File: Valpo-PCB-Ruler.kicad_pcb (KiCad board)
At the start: 2 copper layers, 203.2 x 38.1 mm, 6 parts

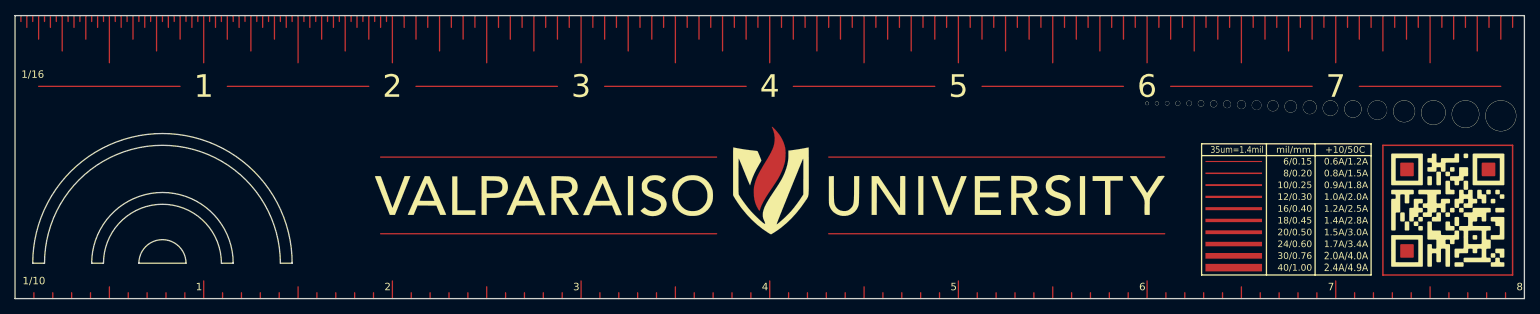
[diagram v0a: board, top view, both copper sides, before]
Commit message: Added Resistor Code + Transistors
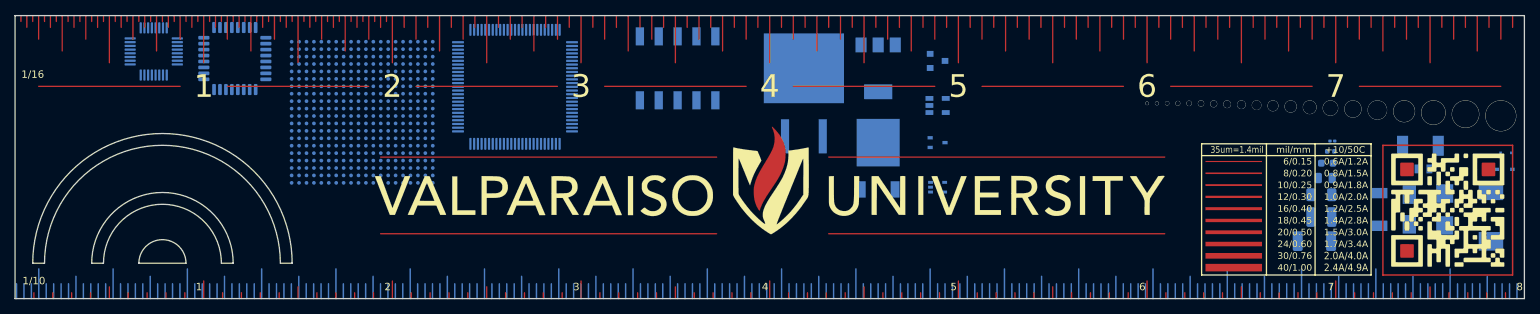
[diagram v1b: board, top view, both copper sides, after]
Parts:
- added 0603: R_0201_0603Metric, Resistor_SMD:R_0201_0603Metric, B.Cu at (228.1, 80.4)
- added 1005: R_0402_1005Metric, Resistor_SMD:R_0402_1005Metric, B.Cu at (227.9, 81.8)
- added 1608: R_0603_1608Metric, Resistor_SMD:R_0603_1608Metric, B.Cu at (227.4, 83.4)
- added 2012: R_0805_2012Metric, Resistor_SMD:R_0805_2012Metric, B.Cu at (227.2, 85.4)
- added 3216: R_1206_3216Metric, Resistor_SMD:R_1206_3216Metric, B.Cu at (226.7, 87.6)
- added 3225: R_1210_3225Metric, Resistor_SMD:R_1210_3225Metric, B.Cu at (226.7, 90.6)
- added 5025: R_2010_5025Metric, Resistor_SMD:R_2010_5025Metric, B.Cu at (225.7, 93.9)
- added BGA 20x20 1.0mm Pitch: BGA-400_21.0x21.0mm_Layout20x20_P1.0mm, Package_BGA:BGA-400_21.0x21.0mm_Layout20x20_P1.0mm, B.Cu at (97.5, 76.5)
- added MELF: D_MELF, Diode_SMD:D_MELF, B.Cu at (240.0, 81.0)
- added MicroMELF: D_MicroMELF, Diode_SMD:D_MicroMELF, B.Cu at (240.4, 84.1)
- added QFP32: LQFP-32_5x5mm_P0.5mm, Package_QFP:LQFP-32_5x5mm_P0.5mm, B.Cu at (69.5, 68.3)
- added QFP32: LQFP-32_7x7mm_P0.8mm, Package_QFP:LQFP-32_7x7mm_P0.8mm, B.Cu at (80.4, 69.3)
- added QPF100: LQFP-100_14x14mm_P0.5mm, Package_QFP:LQFP-100_14x14mm_P0.5mm, B.Cu at (118.1, 73.1)
- added SC80: D_SC-80, Diode_SMD:D_SC-80, B.Cu at (251.5, 82.0)
- added SMA: D_SMA, Diode_SMD:D_SMA, B.Cu at (238.5, 89.6)
- added SMB: D_SMB, Diode_SMD:D_SMB, B.Cu at (243.3, 89.6)
- added SMC: D_SMC, Diode_SMD:D_SMC, B.Cu at (249.5, 90.5)
- added SOD 128: D_SOD-128, Diode_SMD:D_SOD-128, B.Cu at (234.5, 89.6)
- added SOD 323: D_SOD-323, Diode_SMD:D_SOD-323, B.Cu at (251.3, 84.2)
- added SOT223: SOT-223, Package_TO_SOT_SMD:SOT-223, B.Cu at (167.0, 70.6)
- added SOT23: SOT-23, Package_TO_SOT_SMD:SOT-23, B.Cu at (175.0, 69.6)
- added SOT23-5: SOT-23-5, Package_TO_SOT_SMD:SOT-23-5, B.Cu at (175.0, 75.6)
- added SOT323: SOT-353_SC-70-5, Package_TO_SOT_SMD:SOT-353_SC-70-5, B.Cu at (175.0, 86.6)
- added SOT323: SOT-323_SC-70, Package_TO_SOT_SMD:SOT-323_SC-70, B.Cu at (175.0, 80.6)
- added SW_DIP_SPSTx05: SW_DIP_SPSTx05_Slide_9.78x14.88mm_W8.61mm_P2.54mm, Button_Switch_SMD:SW_DIP_SPSTx05_Slide_9.78x14.88mm_W8.61mm_P2.54mm, B.Cu at (140.0, 70.6)
- added TO252: TO-252-2, Package_TO_SOT_SMD:TO-252-2, B.Cu at (167.0, 82.7)
- added TO263: TO-263-2, Package_TO_SOT_SMD:TO-263-2, B.Cu at (157.0, 74.0)
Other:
- board text added: "0"
- board text added: "0.01Ω"
- board text added: "0.05%"
- board text added: "0.10%"
- board text added: "0.1Ω"
- board text added: "0.25%"
- board text added: "0.50%"
- board text added: "0.5mm Pitch"
- board text added: "0.8mm Pitch"
- board text added: "1%"
- board text added: "10%"
- board text added: "100KΩ"
- board text added: "100MΩ"
- board text added: "100Ω"
- board text added: "10KΩ"
- board text added: "10MΩ"
- board text added: "10Ω"
- board text added: "1GΩ"
- board text added: "1KΩ"
- board text added: "1MΩ"
- board text added: "1Ω"
- board text added: "2%"
- board text added: "5%"
- board text added: "Black"
- board text added: "Blue"
- board text added: "Brown"
- board text added: "D2PAK"
- board text added: "DPAK"
- board text added: "Diodes"
- board text added: "Gold"
- board text added: "Green"
- board text added: "Grey"
- board text added: "Orange"
- board text added: "RLC-Metric"
- board text added: "Red"
- board text added: "Resistor Color Code"
- board text added: "SC70"
- board text added: "SC73"
- board text added: "Silver"
- board text added: "Transistors"
- board text added: "Violet"
- board text added: "White"
- board text added: "Yellow"

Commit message: Added Protractor Markings
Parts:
- added G*** (x2): LOGO, Valpo-PCB-Ruler-FP:10_Deg_FP, F.Cu at (73.8, 96.1)
- added G***: LOGO, Valpo-PCB-Ruler-FP:Rest_Deg_FP, F.Cu at (73.8, 96.1)
- added G*** (x2): LOGO, Valpo-PCB-Ruler-FP:COE_FP, F.Cu at (153.0, 94.6)
- moved SW_DIP_SPSTx05 29.1 mm to (118.0, 89.6)
- moved G*** 3.12 mm to (152.4, 82.6)
- moved G*** 3.00 mm to (152.4, 82.7) (x2)
- renumbered SOT323 to SOT353
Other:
- outline, holes or cut-outs redrawn
- board text added: "100"
- board text added: "110"
- board text added: "120"
- board text added: "130"
- board text added: "140"
- board text added: "150"
- board text added: "160"
- board text added: "170"
- board text added: "180"
- board text added: "30"
- board text added: "50"
- board text added: "60"
- board text added: "70"
- board text added: "90"

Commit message: More Back FP and Constants
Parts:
- added 2.5x2: Oscillator_SMD_Abracon_ASDMB-4Pin_2.5x2.0mm, Oscillator:Oscillator_SMD_Abracon_ASDMB-4Pin_2.5x2.0mm, B.Cu at (155.3, 92.6)
- added 3.2x2.4: Oscillator_SMD_EuroQuartz_XO32-4Pin_3.2x2.5mm, Oscillator:Oscillator_SMD_EuroQuartz_XO32-4Pin_3.2x2.5mm, B.Cu at (160.9, 92.6)
- added 5x3.2: Oscillator_SMD_Fordahl_DFAS15-4Pin_5.0x3.2mm, Oscillator:Oscillator_SMD_Fordahl_DFAS15-4Pin_5.0x3.2mm, B.Cu at (174.2, 92.4)
- added 5x3.2: Crystal_SMD_Qantek_QC5CB-2Pin_5x3.2mm, Crystal:Crystal_SMD_Qantek_QC5CB-2Pin_5x3.2mm, B.Cu at (167.3, 92.6)
- added DIP 14 Pin: DIP-14_W7.62mm_SMDSocket_SmallPads, Package_DIP:DIP-14_W7.62mm_SMDSocket_SmallPads, B.Cu at (123.7, 90.3)
- added HC49: Crystal_SMD_HC49-SD_HandSoldering, Crystal:Crystal_SMD_HC49-SD_HandSoldering, B.Cu at (188.3, 93.1)
- added QFN: QFN-20-1EP_3.5x3.5mm_P0.5mm_EP2x2mm, Package_DFN_QFN:QFN-20-1EP_3.5x3.5mm_P0.5mm_EP2x2mm, B.Cu at (108.1, 91.6)
- added QFP: LQFP-32_5x5mm_P0.5mm, Package_QFP:LQFP-32_5x5mm_P0.5mm, B.Cu at (99.0, 92.1)
- added SOIC: SOIC-8_3.9x4.9mm_P1.27mm, Package_SO:SOIC-8_3.9x4.9mm_P1.27mm, B.Cu at (139.4, 93.0)
- added SOT223: SOT-223, Package_TO_SOT_SMD:SOT-223, B.Cu at (157.1, 85.7)
- added SSOP: SSOP-16_4.4x5.2mm_P0.65mm, Package_SO:SSOP-16_4.4x5.2mm_P0.65mm, B.Cu at (148.7, 93.1)
- Dip Switch 5: renamed from SW_DIP_SPSTx05
- moved QPF100 91.0 mm to (208.3, 85.3)
- moved Dip Switch 5 62.4 mm to (57.7, 73.3), turned to 180 degrees
- moved BGA 20x20 1.0mm Pitch 4.82 mm to (102.4, 76.6)
- moved QFP32 3.96 mm to (84.3, 69.7)
- moved QFP32 1.77 mm to (71.1, 69.0)
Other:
- board text added: "-1"
- board text added: "-19"
- board text added: "-2"
- board text added: "-23"
- board text added: "-5"
- board text added: "B"
- board text added: "Boltzmann Const.(k )= 1.381x10 JK"
- board text added: "Boltzmann Const.(k )= 8.617*10 eVK"
- board text added: "Constants"
- board text added: "Coulomb's Const. (k)=8.99×10 Nm C"
- board text added: "Electron Volt(eV)=1.602x10 J"
- board text added: "Elementary Charge(e)=1.602*10 C"
- board text added: "Speed of Light(c)=2.998x10 m/s"
- board text added: "Speed of Sound=343m/s"

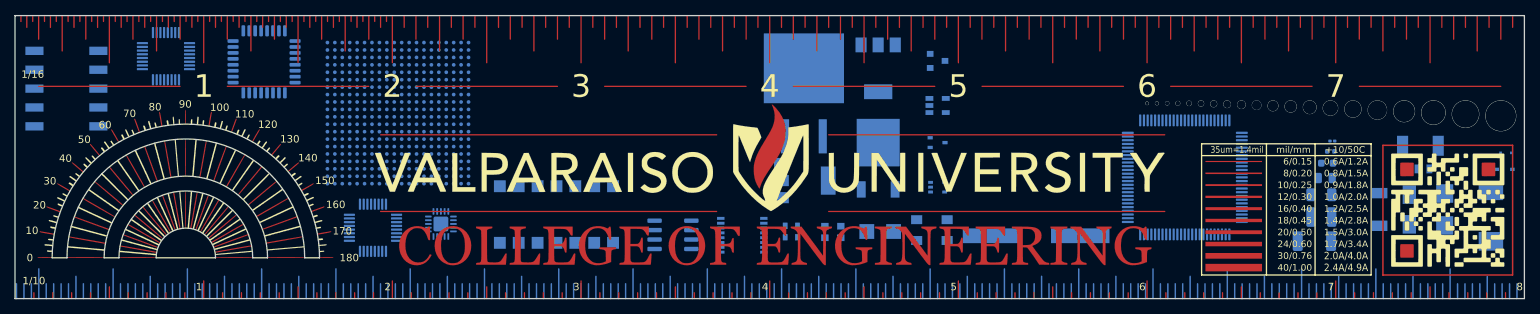
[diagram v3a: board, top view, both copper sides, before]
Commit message: Fixed Front Traces And Rearranged Back
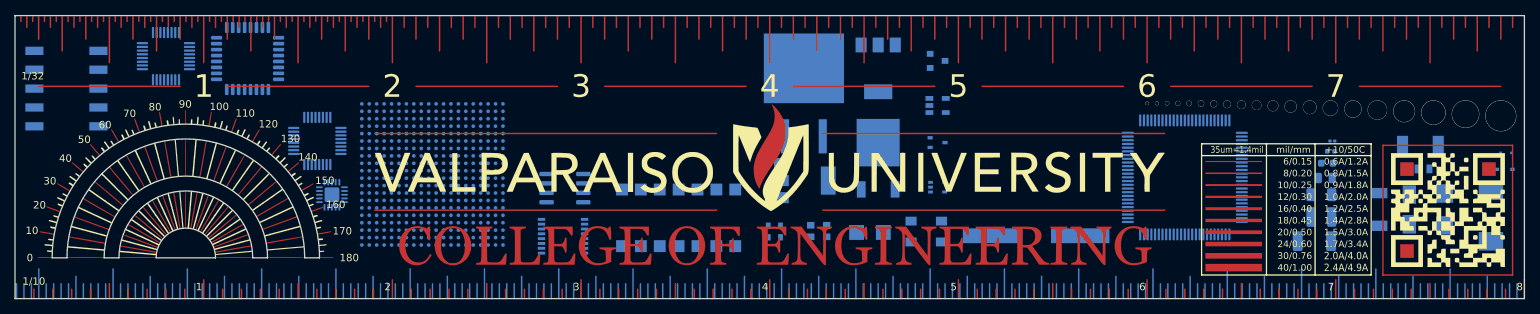
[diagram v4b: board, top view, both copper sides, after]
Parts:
- removed the G*** at (243.7, 89.7) (x3)
- added G*** (x2): LOGO, Valpo-PCB-Ruler-FP:QR_Dots_FP, F.Cu at (243.6, 89.7)
- added G***: LOGO, Valpo-PCB-Ruler-FP:QR_Base_FP, F.Cu at (243.6, 89.7)
- moved SSOP 24.1 mm to (124.6, 93.2)
- moved DIP 14 Pin 16.5 mm to (140.1, 90.7)
- moved SOIC 15.8 mm to (124.8, 86.7)
- moved QFN 15.2 mm to (93.5, 87.6)
- moved QFP 13.9 mm to (91.5, 80.4)
- moved BGA 20x20 1.0mm Pitch 9.47 mm to (107.0, 84.9)
- moved 2.5x2 2.29 mm to (153.0, 92.6)
- moved QFP32 2.27 mm to (82.1, 69.3)
- moved 3.2x2.4 1.91 mm to (159.0, 92.5)
- moved 5x3.2 1.38 mm to (165.9, 92.7)
- moved 5x3.2 0.79 mm to (173.5, 92.6)
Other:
- board text added: "-12"
- board text added: "-6"
- board text added: "1/32"
- board text added: "Coulomb's Const.(k)=8.99×10 Nm C"
- board text added: "Elementary Charge(q)=1.602*10 C"
- board text added: "Vacuum Permeability(μ )=1.257x10 H/m"
- board text added: "Vacuum Permittivity(ε )=8.854x10 Fm"
- board text removed: "-5"
- board text removed: "1/16"
- board text removed: "Boltzmann Const.(k )= 8.617*10 eVK"
- board text removed: "Coulomb's Const. (k)=8.99×10 Nm C"
- board text removed: "Elementary Charge(e)=1.602*10 C"

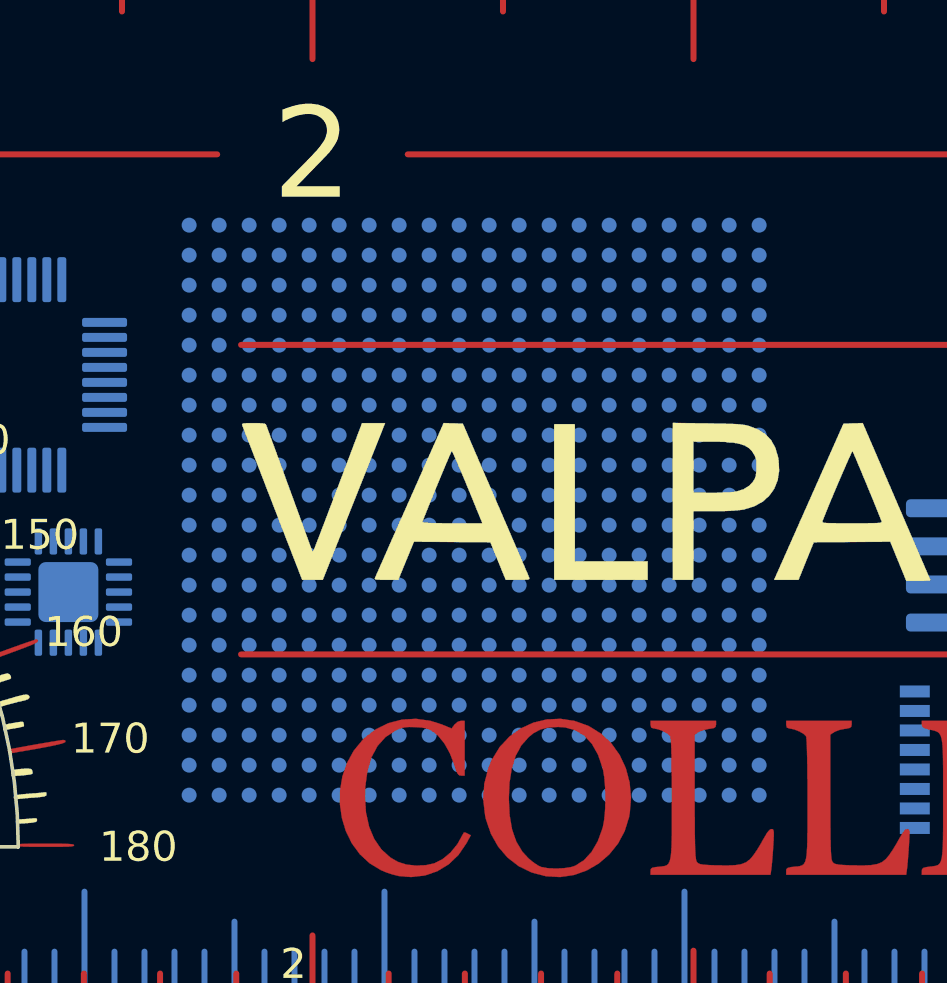
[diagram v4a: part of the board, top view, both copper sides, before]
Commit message: Conversions Added/ Fixed QR Code
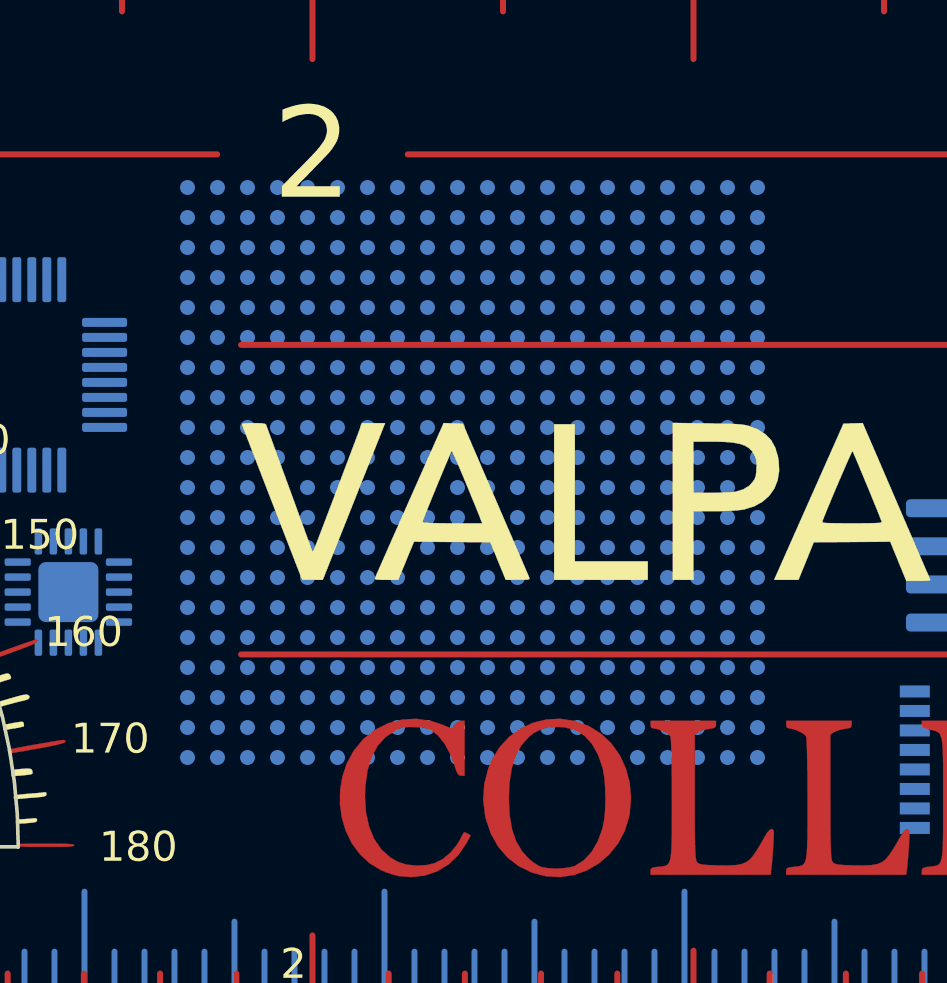
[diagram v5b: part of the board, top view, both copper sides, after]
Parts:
- moved BGA 20x20 1.0mm Pitch 1.26 mm to (106.9, 83.6)
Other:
- board text added: "Conversions"
- board text added: "L=gallons×3.785"
- board text added: "Nm=ftlb×1.3558"
- board text added: "cm=inches×2.54"
- board text added: "kg=lbs×0.454"
- board text added: "km=miles×1.609"
- board text added: "°C=(°F-32)×5/9"
- board text added: "°C=K-273.15"
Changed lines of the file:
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@@
   (general
     (thickness 1.6)
-    (drawings 1224)
+    (drawings 1237)
     (tracks 20)
     (zones 0)
@@
   (page A4)
   (layers
-    (0 F.Cu signal)
-    (31 B.Cu signal hide)
+    (0 F.Cu signal hide)
+    (31 B.Cu signal)
     (32 B.Adhes user hide)
     (33 F.Adhes user hide)
     (34 B.Paste user hide)
     (35 F.Paste user hide)
-    (36 B.SilkS user hide)
-    (37 F.SilkS user)
-    (38 B.Mask user hide)
-    (39 F.Mask user)
+    (36 B.SilkS user)
+    (37 F.SilkS user hide)
+    (38 B.Mask user)
+    (39 F.Mask user hide)
     (40 Dwgs.User user)
     (41 Cmts.User user hide)
@@
   )
   (module Package_BGA:BGA-400_21.0x21.0mm_Layout20x20_P1.0mm (layer B.Cu)
-    (at 106.9885 84.8845)
+    (at 106.934 83.6295)
     (descr "BGA-400, https://www.xilinx.com/support/documentation/package_specs/fg400.pdf")
     (tags BGA-400)
     (attr smd)
-    (fp_text reference "BGA 20x20 1.0mm Pitch" (at -0.1905 -11.7475) (layer B.SilkS)
+    (fp_text reference "BGA 20x20 1.0mm Pitch" (at 0 11.43) (layer B.SilkS)
       (effects (font (size 1 1) (thickness 0.15)) (justify mirror))
     )
@@
       (xy -4.88682 -4.482967) (xy -4.876452 -4.486047) (xy -4.871357 -4.484994)) (layer F.SilkS) (width 0.01))
   )
+  (gr_text "L=gallons×3.785\n" (at 103.9495 70.9295) (layer B.SilkS)
+    (effects (font (size 1 1) (thickness 0.15)) (justify left mirror))
+  )
+  (gr_text "Nm=ftlb×1.3558\n" (at 103.9495 68.918666) (layer B.SilkS)
+    (effects (font (size 1 1) (thickness 0.15)) (justify left mirror))
+  )
+  (gr_text °C=K-273.15 (at 103.9495 66.907833) (layer B.SilkS)
+    (effects (font (size 1 1) (thickness 0.15)) (justify left mirror))
+  )
+  (gr_text "°C=(°F-32)×5/9" (at 103.9495 64.897) (layer B.SilkS)
+    (effects (font (size 1 1) (thickness 0.15)) (justify left mirror))
+  )
+  (gr_text kg=lbs×0.454 (at 118.26875 70.866) (layer B.SilkS)
+    (effects (font (size 1 1) (thickness 0.15)) (justify left mirror))
+  )
+  (gr_text km=miles×1.609 (at 118.26875 68.67525) (layer B.SilkS)
+    (effects (font (size 1 1) (thickness 0.15)) (justify left mirror))
+  )
+  (gr_text "cm=inches×2.54\n" (at 118.26875 66.4845) (layer B.SilkS)
+    (effects (font (size 1 1) (thickness 0.15)) (justify left mirror))
+  )
+  (gr_line (start 104.648 70.77075) (end 104.648 65.2145) (layer B.SilkS) (width 0.12))
+  (gr_line (start 118.4275 65.263) (end 109.474 65.263) (layer B.SilkS) (width 0.12))
+  (gr_text Conversions (at 114.1095 64.501) (layer B.SilkS)
+    (effects (font (size 1 1) (thickness 0.15)) (justify mirror))
+  )
+  (gr_line (start 88.9 71.4375) (end 88.9 64.29375) (layer B.SilkS) (width 0.12))
+  (gr_line (start 118.26875 72.23125) (end 89.69375 72.23125) (layer B.SilkS) (width 0.12))
+  (gr_line (start 119.0625 64.29375) (end 119.0625 71.4375) (layer B.SilkS) (width 0.12))
   (gr_line (start 145.25625 89.69375) (end 99.21875 89.69375) (layer F.Cu) (width 0.2))
   (gr_line (start 145.25625 89.69375) (end 99.21875 89.69375) (layer F.Mask) (width 0.2))
